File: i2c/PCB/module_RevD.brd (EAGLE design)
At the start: 33.3 x 50.2 mm, 131 parts, among them IC1 ATTINY85-20SU, J1 M20-9980346

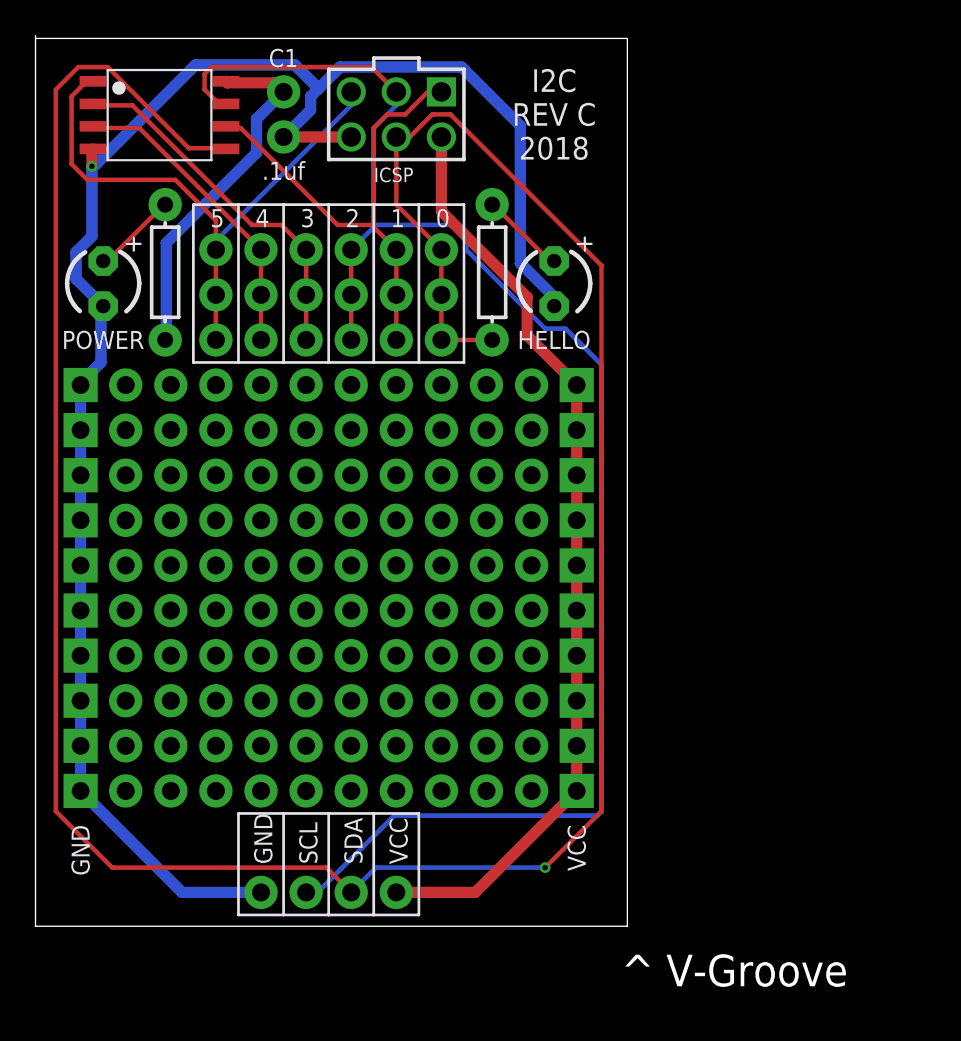
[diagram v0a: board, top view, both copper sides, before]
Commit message: smaller proto pads, improved routing
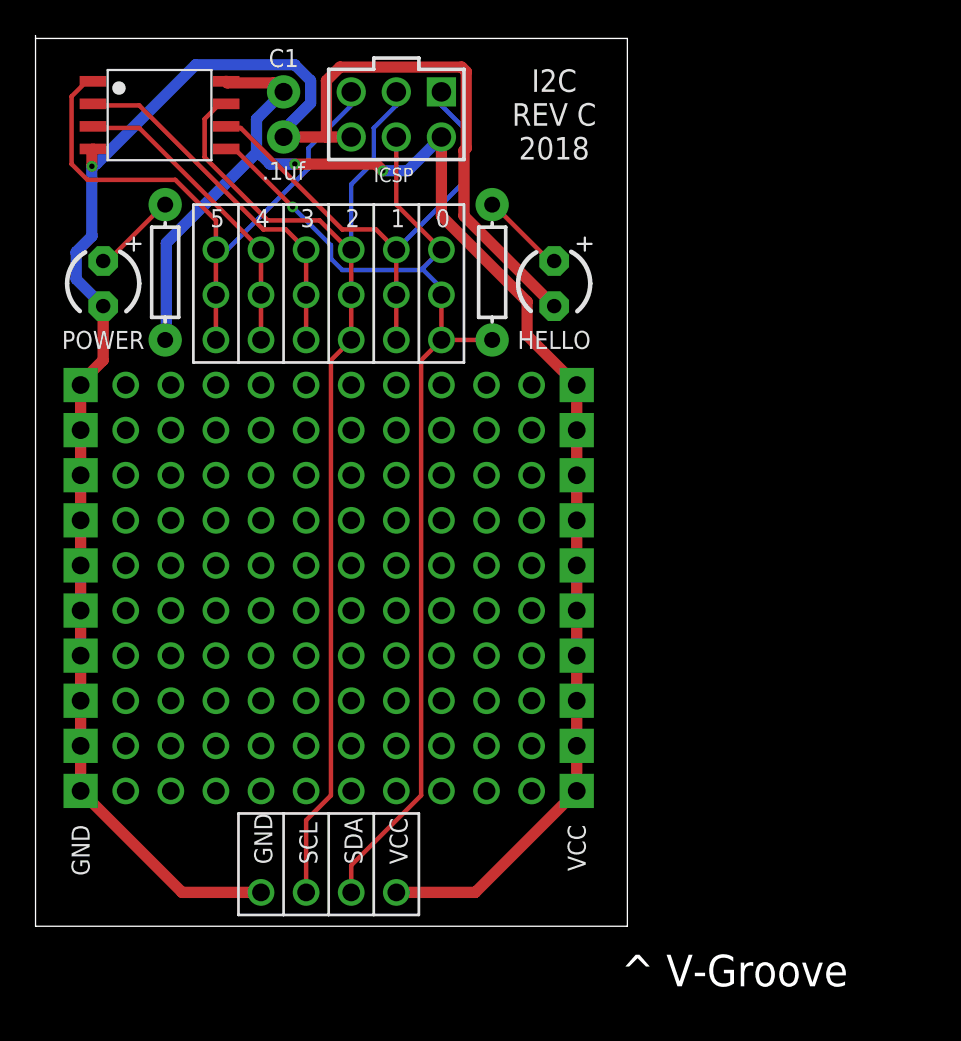
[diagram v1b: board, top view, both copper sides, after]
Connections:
- net GND: now also U$71.P$1; no longer U$71.1
- net PB0: now also U$72.P$1, U$75.P$1, U$76.P$1, U$77.P$1; no longer U$72.1, U$75.1, U$76.1, U$77.1
- net PB1: now also U$78.P$1, U$79.P$1, U$80.P$1; no longer U$78.1, U$79.1, U$80.1
- net PB2: now also U$73.P$1, U$81.P$1, U$82.P$1, U$83.P$1; no longer U$73.1, U$81.1, U$82.1, U$83.1
- net PB3: now also U$84.P$1, U$85.P$1, U$86.P$1; no longer U$84.1, U$85.1, U$86.1
- net PB4: now also U$87.P$1, U$88.P$1, U$89.P$1; no longer U$87.1, U$88.1, U$89.1
- net PB5: now also U$90.P$1, U$91.P$1, U$92.P$1; no longer U$90.1, U$91.1, U$92.1
- net VCC: now also U$74.P$1; no longer U$74.1
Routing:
- net PB0: track 148.9 -> 63.8 mm
- net PB2: track 89.1 -> 61.3 mm
- net VCC: track 72.8 -> 84.4 mm, vias 0 -> 2
- net GND: track 97.4 -> 99.7 mm
- net PB1: track 27.8 -> 28.5 mm
